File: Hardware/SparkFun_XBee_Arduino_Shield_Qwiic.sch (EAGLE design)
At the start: 82 parts, among them J4 QWIIC_RIGHT_ANGLE, Q1 20V/4.2A/52mΩ/1.4W, Q2 20V/4.2A/52mΩ/1.4W, Q3 3.1A/30V/105mΩ, Q4 5.8A/30V/35mΩ, Q5 20V/4.2A/52mΩ/1.4W, U1 FSUSB30MUX_MSOP10, U2 AP63203, U3 ESD Diode, U4 FT231XS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

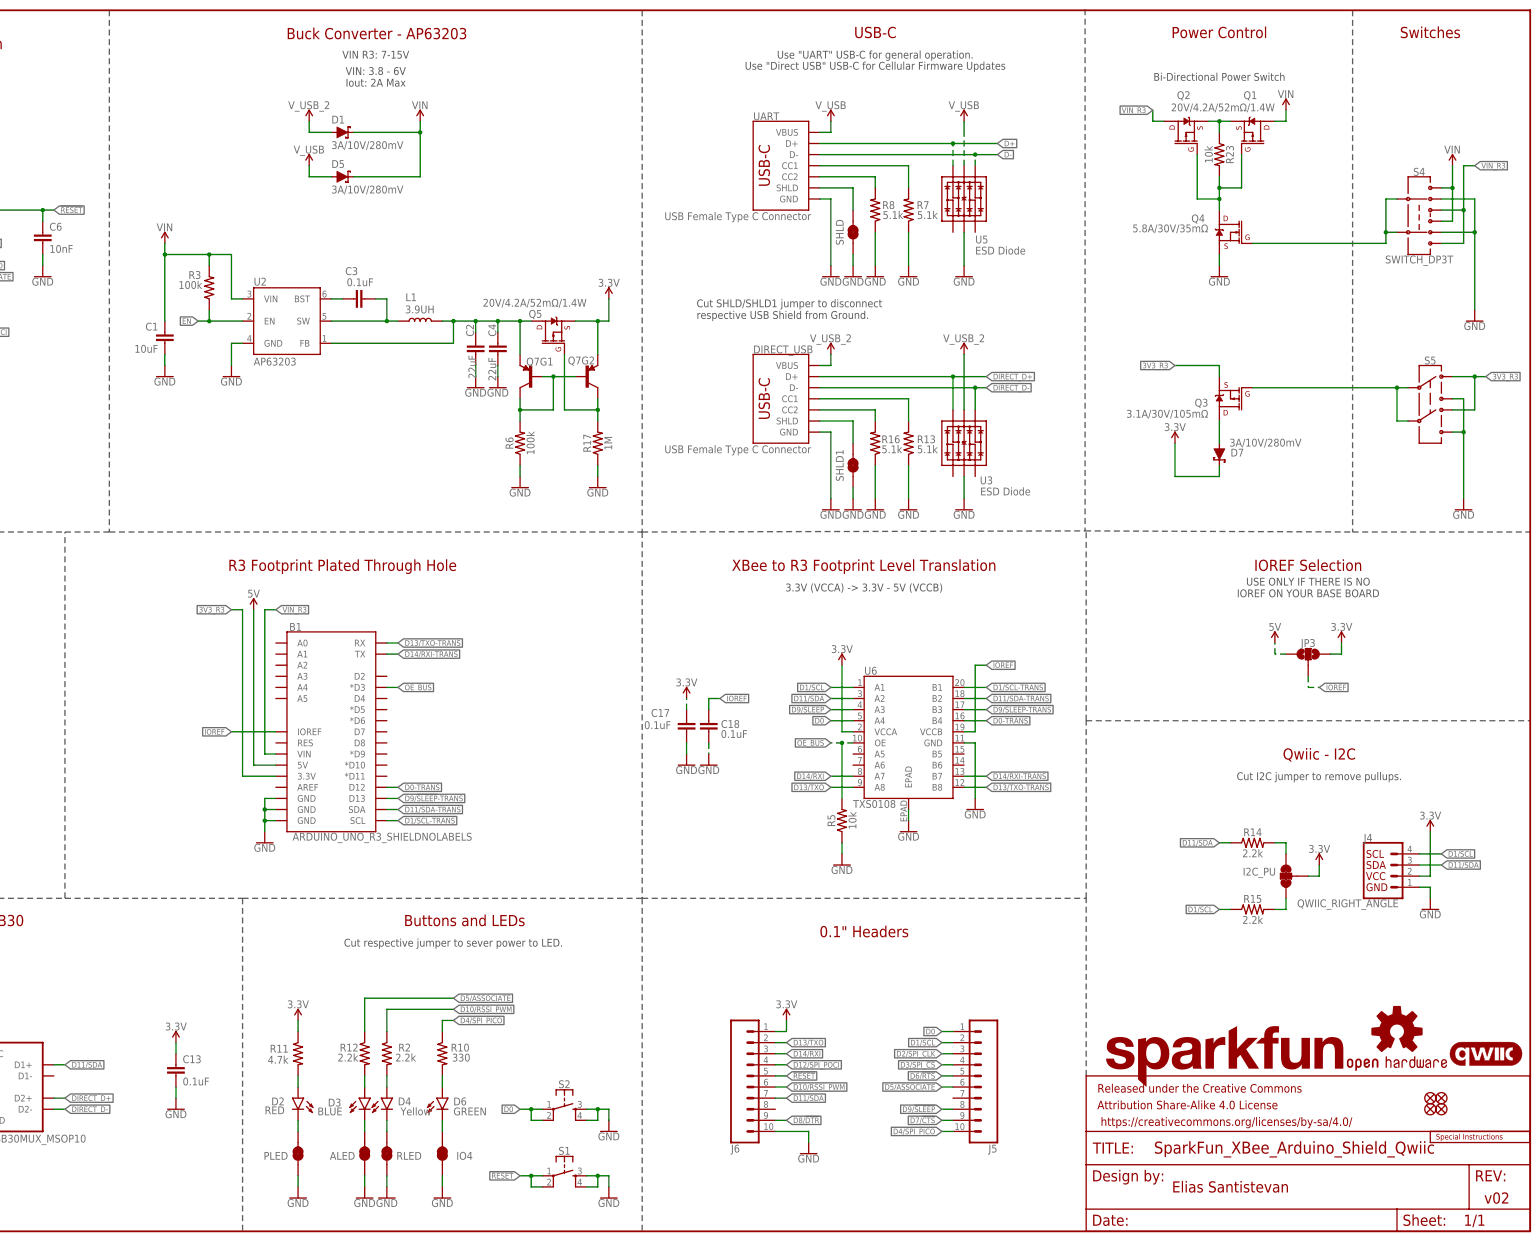
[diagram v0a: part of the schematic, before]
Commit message: v03 changes
* Replaces bi-directional power switch with jumper
* Removes level translators
* Removes a majority of nets connecting to R3 PTH
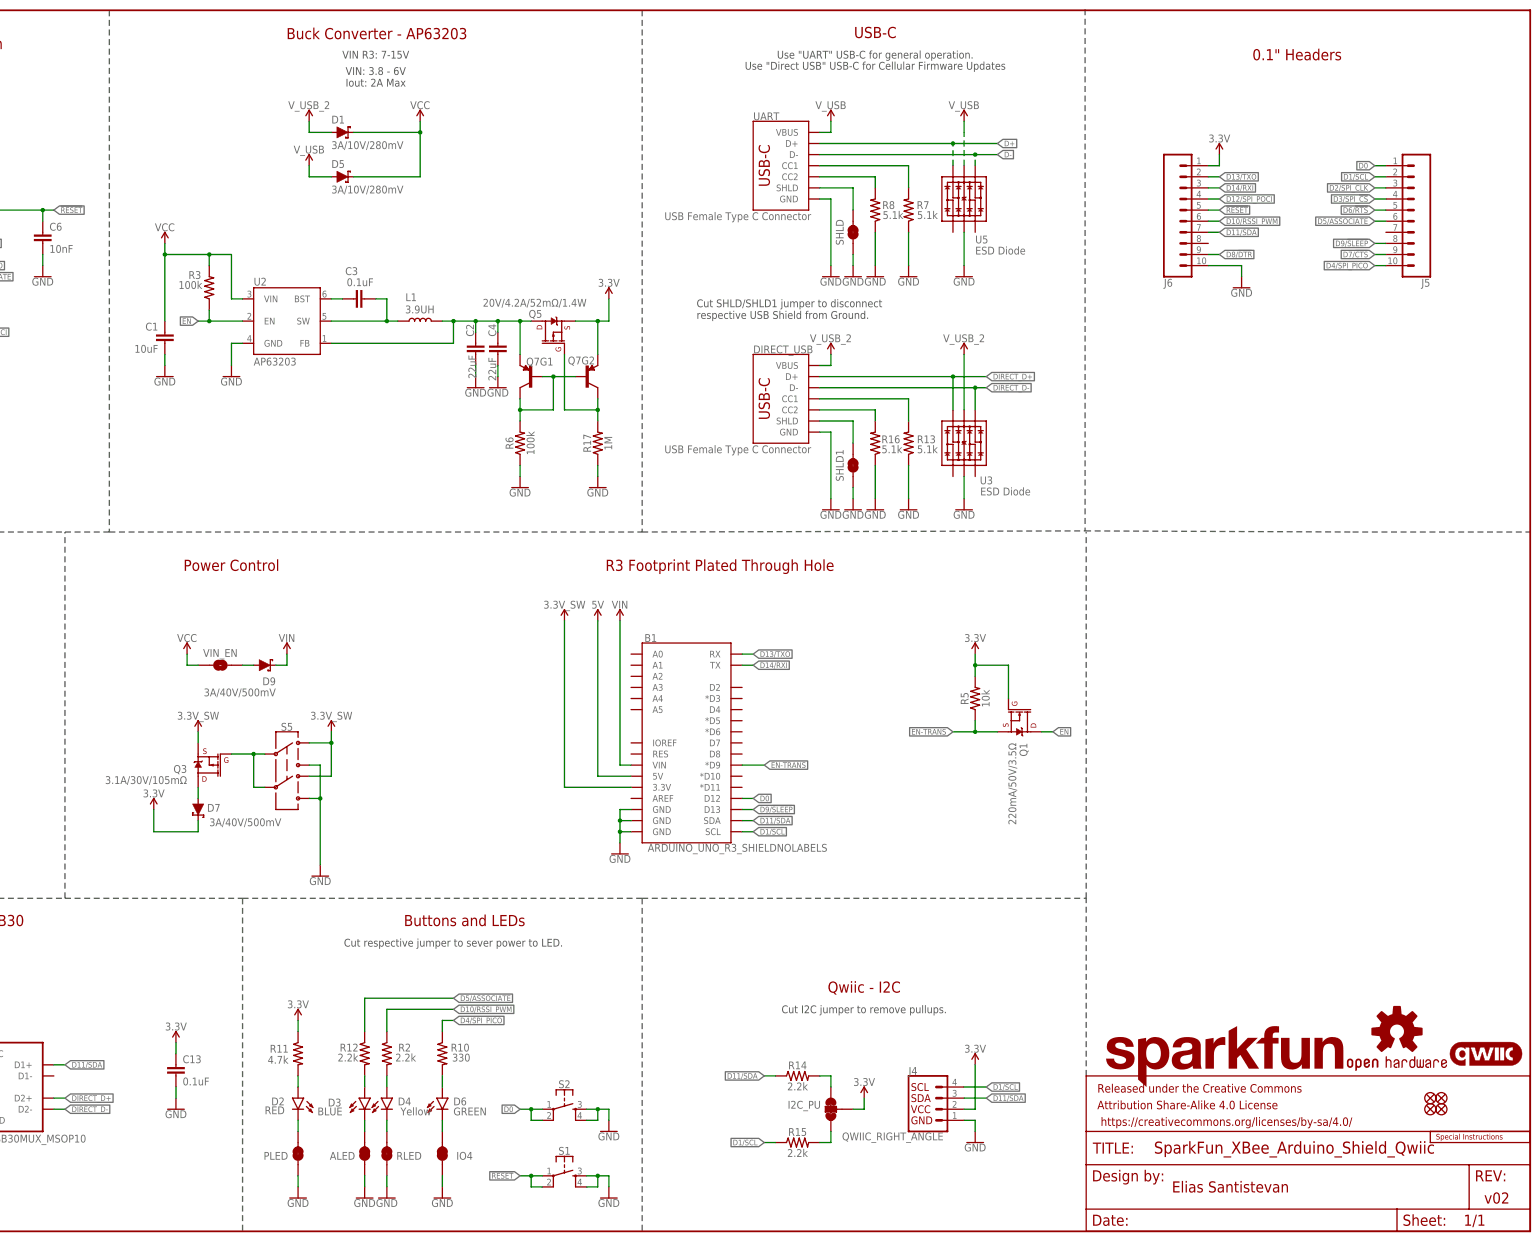
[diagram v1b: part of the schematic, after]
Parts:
- removed C17, C18: 0.1uF, SparkFun-Capacitors:0.1UF-0603-25V-(+80/-20%)
- removed JP3: JUMPER-SMT_3_NO_SILK, SparkFun-Jumpers:JUMPER-SMT_3_NO_SILK
- removed Q2: 20V/4.2A/52mΩ/1.4W, SparkFun-DiscreteSemi:MOSFET_PCH-DMG2305UX-7
- removed Q4: 5.8A/30V/35mΩ, SparkFun-DiscreteSemi:MOSFET-NCH-AO3404A
- removed R23: 10k, SparkFun-Resistors:10KOHM-0603-1/10W-1%
- removed S4: SWITCH_DP3T, DP3T:SWITCH_DP3T
- removed U6: TXS0108, SparkFun-IC-Comms:TXS0108-VFQFN_20
- added D9: 3A/40V/500mV, SparkFun-DiscreteSemi:DIODE-SCHOTTKY-B340A
- added VIN_EN: JUMPER-SMT_2_NO_SILK, SparkFun-Jumpers:JUMPER-SMT_2_NO_SILK
- D7: value 3A/10V/280mV -> 3A/40V/500mV; device SparkFun-DiscreteSemi:DIODE-SCHOTTKY-BAT60A -> SparkFun-DiscreteSemi:DIODE-SCHOTTKY-B340A
- Q1: value 20V/4.2A/52mΩ/1.4W -> 220mA/50V/3.5Ω; device SparkFun-DiscreteSemi:MOSFET_PCH-DMG2305UX-7 -> SparkFun-DiscreteSemi:MOSFET-NCH-BSS138
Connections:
- net 3V3_R3 renamed 3.3V_SW
- removed net D0-TRANS: B1.D12, U6.B4
- removed net D1/SCL-TRANS: B1.SCL, U6.B1
- removed net D11/SDA-TRANS: B1.SDA, U6.B2
- removed net D13/TXO-TRANS: B1.RX, U6.B8
- removed net D14/RXI-TRANS: B1.TX, U6.B7
- removed net D9/!SLEEP!-TRANS: B1.D13, U6.B3
- removed net GATE: Q1.G, Q2.G, Q4.D, R23.2
- removed net IOREF: B1.IOREF, C18.1, JP3.2, U6.VCCB
- removed net N$22: Q4.G, S4.3, S4.7
- removed net OE_BUS: B1.*D3, R5.2, U6.OE
- removed net SOURCE: Q1.S, Q2.S, R23.1
- removed net VIN_R3: B1.VIN, Q2.D, S4.1, S4.5
- new net EN-TRANS: B1.*D9, Q1.S, R5.1
- new net N$9: D9.A, VIN_EN.2
- new net VCC: C1.1, D1.C, D5.C, R3.2, U2.VIN, VIN_EN.1
- net 3.3V: now also Q1.G, R5.2; no longer C17.1, JP3.1, U6.VCCA
- net 5V: no longer JP3.3
- net D0: now also B1.D12; no longer U6.A4
- net D1/SCL: now also B1.SCL; no longer U6.A1
- net D11/SDA: now also B1.SDA; no longer U6.A2
- net D13/TXO: now also B1.RX; no longer U6.A8
- net D14/RXI: now also B1.TX; no longer U6.A7
- net D9/!SLEEP!: now also B1.D13; no longer U6.A3
- net EN: now also Q1.D
- net GND: no longer C17.2, C18.2, Q4.S, R5.1, S4.2, S4.6, U6.EPAD, U6.GND
- net VIN: now also B1.VIN, D9.C; no longer C1.1, D1.C, D5.C, Q1.D, R3.2, S4.4, S4.8, U2.VIN
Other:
- note removed: "3.3V (VCCA) -> 3.3V - 5V (VCCB)"
- note removed: "Bi-Directional Power Switch"
- note removed: "IOREF Selection"
- note removed: "Switches"
- note removed: "USE ONLY IF THERE IS NO IOREF ON YOUR BASE BOARD"
- note removed: "XBee to R3 Footprint Level Translation"
- moved on the sheet: B1, D7, I2C_PU, J4, J5, J6, Q3, R14, R15, R5, S5

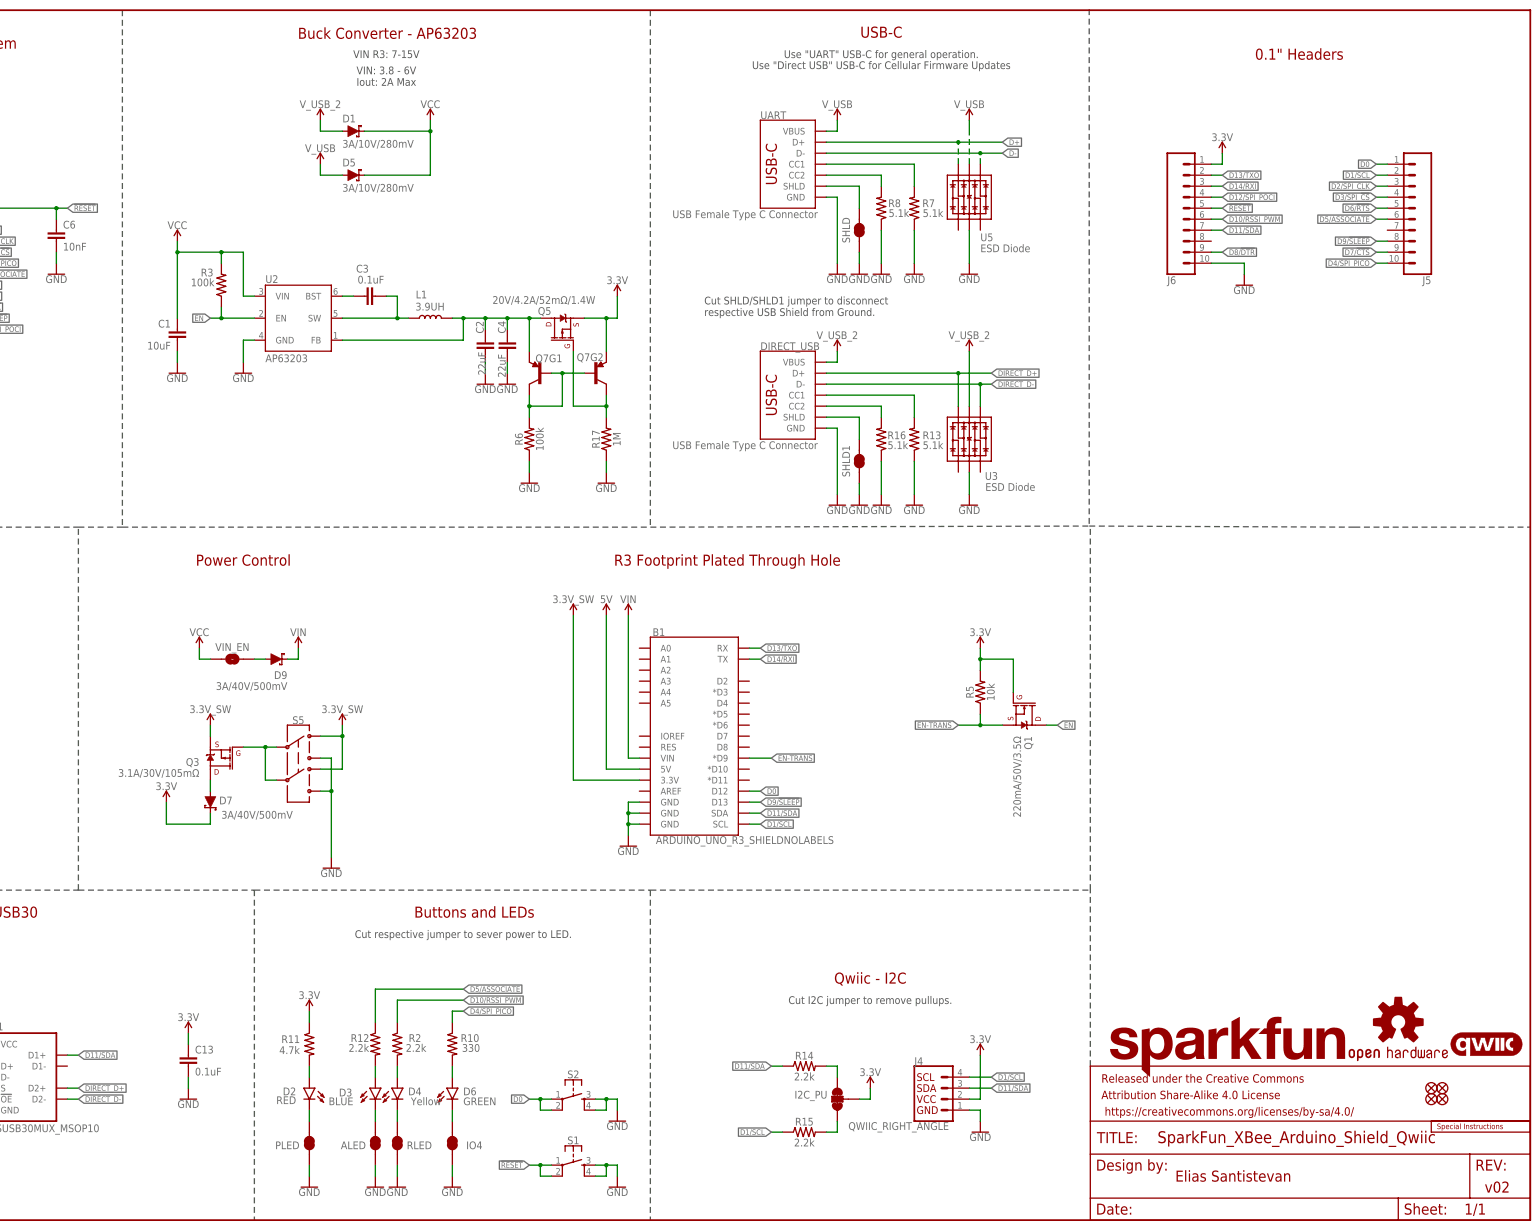
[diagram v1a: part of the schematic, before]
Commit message: Optimizes traces
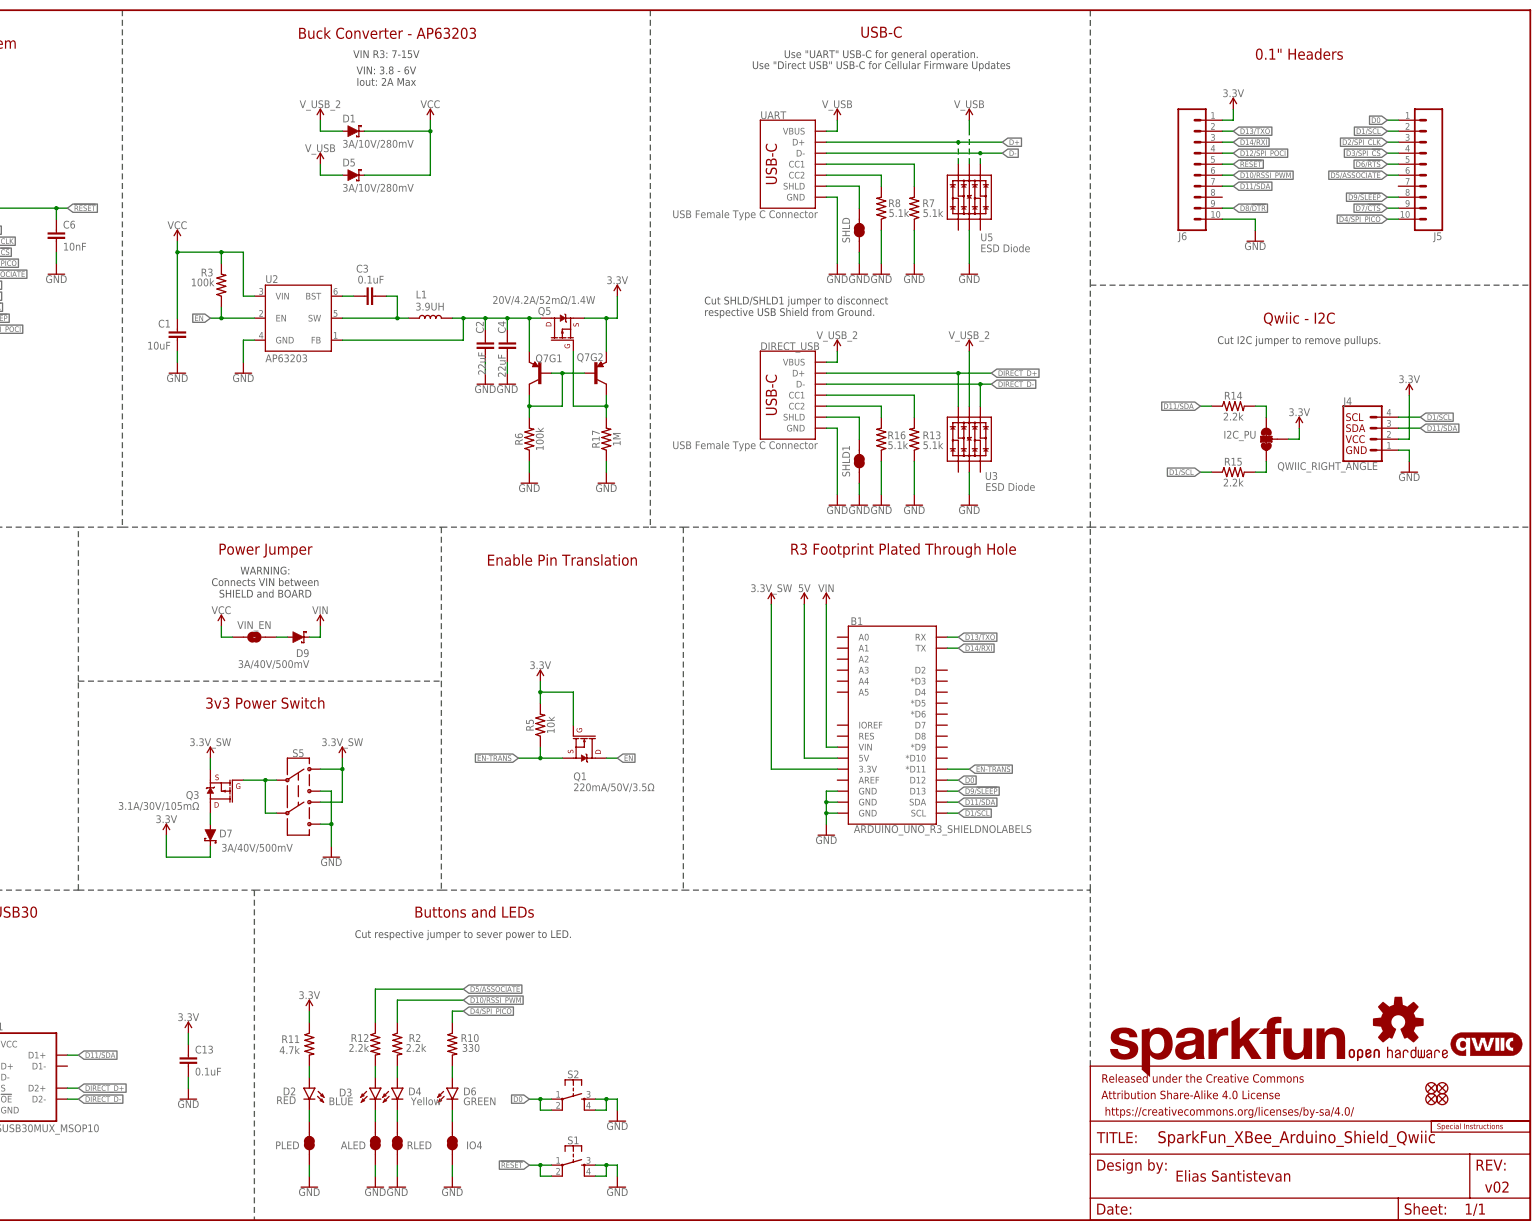
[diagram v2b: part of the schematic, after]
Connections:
- net EN-TRANS: now also B1.*D11; no longer B1.*D9
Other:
- note added: "3v3 Power Switch"
- note added: "Enable Pin Translation"
- note added: "Power Jumper"
- note added: "WARNING: Connects VIN between SHIELD and BOARD"
- note removed: "Power Control"
- moved on the sheet: B1, D7, D9, I2C_PU, J4, J5, J6, Q1, Q3, R14, R15, R5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

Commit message: Improves spacing in schematic
* Improves ground pour
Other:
- note added: "v03"
- note removed: "v02"
- moved on the sheet: ALED, C11, C12, C14, D2, D3, D4, D6, IO4, PLED, R10, R11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

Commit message: Adds silk and vias
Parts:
- renumbered VIN_EN to X1
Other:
- note added: "WARNING: X1 Jumper connects VIN between SHIELD and BOARD"
- note removed: "WARNING: Connects VIN between SHIELD and BOARD"
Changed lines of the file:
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@@
 <part name="GND44" library="SparkFun-PowerSymbols" deviceset="GND" device=""/>
 <part name="D7" library="SparkFun-DiscreteSemi" deviceset="DIODE-SCHOTTKY" device="-B340A" value="3A/40V/500mV"/>
-<part name="VIN_EN" library="SparkFun-Jumpers" deviceset="JUMPER-SMT_2_NO" device="_SILK" package3d_urn="urn:adsk.eagle:package:39279/1"/>
+<part name="X1" library="SparkFun-Jumpers" deviceset="JUMPER-SMT_2_NO" device="_SILK" package3d_urn="urn:adsk.eagle:package:39279/1"/>
 <part name="D9" library="SparkFun-DiscreteSemi" deviceset="DIODE-SCHOTTKY" device="-B340A" value="3A/40V/500mV"/>
 <part name="SUPPLY2" library="SparkFun-PowerSymbols" deviceset="VCC" device=""/>
@@
 <wire x1="96.52" y1="124.46" x2="180.34" y2="124.46" width="0.2032" layer="97" style="longdash"/>
 <text x="139.7" y="147.32" size="1.778" layer="97" font="vector" align="center">WARNING:
-Connects VIN between
+X1 Jumper connects VIN between
 SHIELD and BOARD</text>
 <wire x1="330.2" y1="215.9" x2="431.8" y2="215.9" width="0.2032" layer="97" style="longdash"/>
@@
 <attribute name="VALUE" x="129.54" y="86.868" size="1.778" layer="96" font="vector" align="top-left"/>
 </instance>
-<instance part="VIN_EN" gate="G$1" x="137.16" y="134.62" smashed="yes">
+<instance part="X1" gate="G$1" x="137.16" y="134.62" smashed="yes">
 <attribute name="NAME" x="137.16" y="137.414" size="1.778" layer="95" font="vector" align="center"/>
 </instance>
@@
 <net name="VCC" class="0">
 <segment>
-<pinref part="VIN_EN" gate="G$1" pin="1"/>
+<pinref part="X1" gate="G$1" pin="1"/>
 <wire x1="132.08" y1="134.62" x2="129.54" y2="134.62" width="0.1524" layer="91"/>
 <wire x1="129.54" y1="134.62" x2="129.54" y2="137.16" width="0.1524" layer="91"/>
@@
 <net name="N$9" class="0">
 <segment>
-<pinref part="VIN_EN" gate="G$1" pin="2"/>
+<pinref part="X1" gate="G$1" pin="2"/>
 <pinref part="D9" gate="G$1" pin="A"/>
 <wire x1="142.24" y1="134.62" x2="144.78" y2="134.62" width="0.1524" layer="91"/>
